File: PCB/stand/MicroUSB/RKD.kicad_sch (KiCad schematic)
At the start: 63 parts, among them J1 USB_B_Micro, J10 Conn_01x04_Male, J11 Conn_02x06_Odd_Even, J12 Conn_01x06, J13 Conn_01x03, J14 Conn_01x04, J15 Conn_01x04, J2 Conn_02x02_Odd_Even, J3 Conn_02x04_Odd_Even, J4 Conn_02x02_Odd_Even, J5 Conn_02x04_Odd_Even, K1 Key, K2 Key, K3 Key, K4 Key, SW2 SW_DIP_x04, SW3 SW_Push, SW5 SW_Push, U1 W25Q32JV, U2 RP2040, U3 CH9329, U4 AMS1117-33, Y1 Crystal 12MHZ HC49, Y2 Crystal_GND24 12MHZ 3225

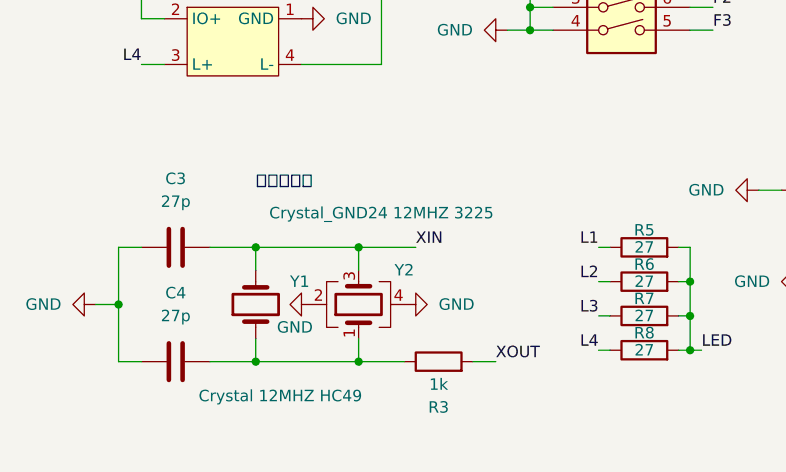
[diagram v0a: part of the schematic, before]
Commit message: 紧急修复:经验证3225晶振无法稳定起振,故去除所以文件中的3225晶振
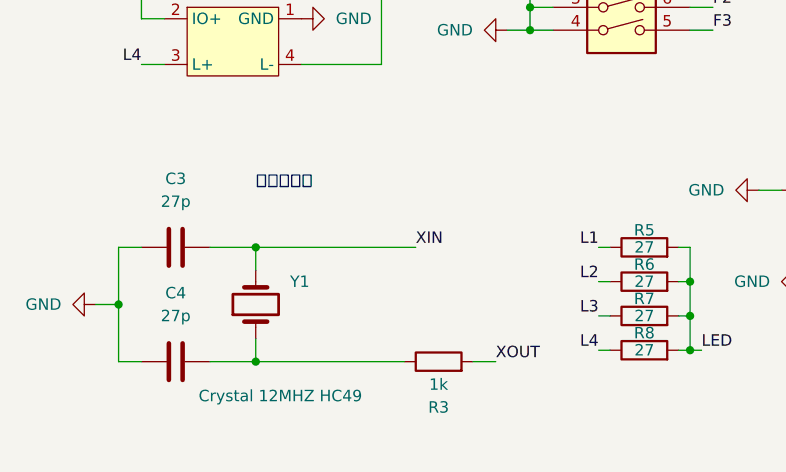
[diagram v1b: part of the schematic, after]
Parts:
- removed Y2: Crystal_GND24 12MHZ 3225, Crystal:Crystal_SMD_3225-4Pin_3.2x2.5mm, symbol Device:Crystal_GND24

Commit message: rename
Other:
- company: PCX-LK -> PTALTS-LK
